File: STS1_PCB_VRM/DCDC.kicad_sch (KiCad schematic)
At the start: 25 parts, among them Q2 BSS123, U6 MP28167GQ

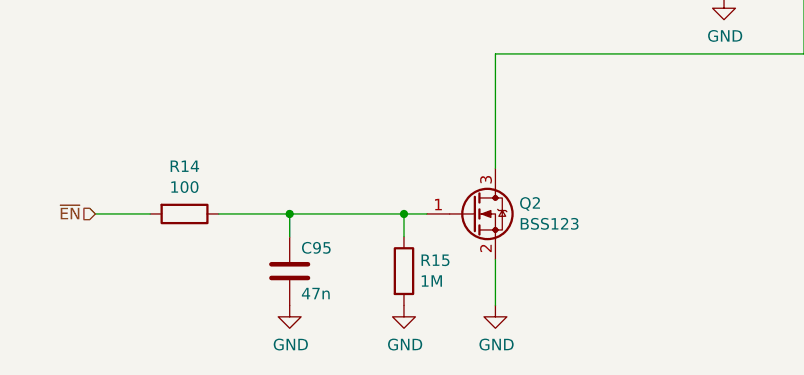
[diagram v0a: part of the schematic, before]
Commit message: Add a couple of Zener diodes to protect inputs of MOSFETs
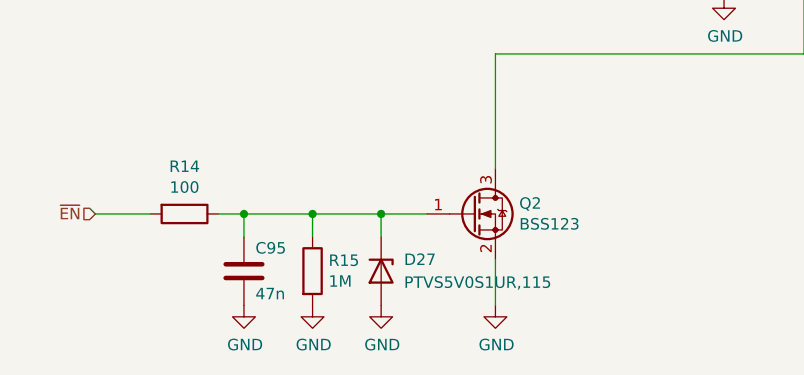
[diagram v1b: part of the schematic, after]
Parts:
- added D27: PTVS5V0S1UR,115, Diode_SMD:D_SOD-123, symbol Device:D_Zener
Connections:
- net GND: now also D27.2 (A)
- net at C95.1, Q2.1 (G), R14.1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: now also D27.1 (K)
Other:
- moved on the sheet: C95, R15
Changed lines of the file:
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@@
 (kicad_sch (version 20211123) (generator eeschema)
   (paper "A4")
-  (junction (at 57.15 102.87) (diameter 0) (color 0 0 0 0)
-  )
   (junction (at 125.73 96.52) (diameter 0) (color 0 0 0 0)
   )
@@
   (junction (at 105.41 73.66) (diameter 0) (color 0 0 0 0)
   )
+  (junction (at 54.61 102.87) (diameter 0) (color 0 0 0 0)
+  )
   (junction (at 105.41 60.96) (diameter 0) (color 0 0 0 0)
   )
+  (junction (at 46.99 102.87) (diameter 0) (color 0 0 0 0)
+  )
   (junction (at 238.76 82.55) (diameter 0) (color 0 0 0 0)
   )
+  (junction (at 39.37 102.87) (diameter 0) (color 0 0 0 0)
+  )
   (junction (at 114.3 73.66) (diameter 0) (color 0 0 0 0)
   )
   (junction (at 82.55 60.96) (diameter 0) (color 0 0 0 0)
   )
-  (junction (at 44.45 102.87) (diameter 0) (color 0 0 0 0)
-  )
   (junction (at 181.61 66.04) (diameter 0) (color 0 0 0 0)
   )
@@
   (junction (at 92.71 60.96) (diameter 0) (color 0 0 0 0)
   )
+  (wire (pts (xy 54.61 102.87) (xy 54.61 105.41))
+    (stroke (width 0) (type default) (color 0 0 0 0))
+  )
   (wire (pts (xy 179.07 77.47) (xy 194.31 77.47))
     (stroke (width 0) (type default) (color 0 0 0 0))
@@
     (stroke (width 0) (type default) (color 0 0 0 0))
   )
-  (wire (pts (xy 44.45 102.87) (xy 57.15 102.87))
-    (stroke (width 0) (type default) (color 0 0 0 0))
-  )
   (wire (pts (xy 191.77 82.55) (xy 203.2 82.55))
     (stroke (width 0) (type default) (color 0 0 0 0))
@@
     (stroke (width 0) (type default) (color 0 0 0 0))
   )
-  (wire (pts (xy 36.576 102.87) (xy 44.45 102.87))
+  (wire (pts (xy 46.99 102.87) (xy 54.61 102.87))
+    (stroke (width 0) (type default) (color 0 0 0 0))
+  )
+  (wire (pts (xy 36.576 102.87) (xy 39.37 102.87))
     (stroke (width 0) (type default) (color 0 0 0 0))
   )
@@
     (stroke (width 0) (type default) (color 0 0 0 0))
   )
+  (wire (pts (xy 54.61 102.87) (xy 59.69 102.87))
+    (stroke (width 0) (type default) (color 0 0 0 0))
+  )
   (wire (pts (xy 54.61 63.5) (xy 54.61 60.96))
     (stroke (width 0) (type default) (color 0 0 0 0))
@@
     (stroke (width 0) (type default) (color 0 0 0 0))
   )
+  (wire (pts (xy 39.37 102.87) (xy 46.99 102.87))
+    (stroke (width 0) (type default) (color 0 0 0 0))
+  )
   (wire (pts (xy 105.41 73.66) (xy 114.3 73.66))
     (stroke (width 0) (type default) (color 0 0 0 0))
@@
     (stroke (width 0) (type default) (color 0 0 0 0))
   )
-  (wire (pts (xy 44.45 102.87) (xy 44.45 105.41))
+  (wire (pts (xy 39.37 102.87) (xy 39.37 105.41))
     (stroke (width 0) (type default) (color 0 0 0 0))
   )
@@
     (stroke (width 0) (type default) (color 0 0 0 0))
   )
-  (wire (pts (xy 57.15 102.87) (xy 59.69 102.87))
-    (stroke (width 0) (type default) (color 0 0 0 0))
-  )
-  (wire (pts (xy 57.15 105.41) (xy 57.15 102.87))
+  (wire (pts (xy 46.99 105.41) (xy 46.99 102.87))
     (stroke (width 0) (type default) (color 0 0 0 0))
   )
@@
     (pin "2")
   )
-  (symbol (lib_id "Device:R") (at 57.15 109.22 0) (unit 1)
-    (in_bom yes) (on_board yes)
-    (property "Reference" "R15" (id 0) (at 58.928 108.0516 0)
-      (effects (font (size 1.27 1.27)) (justify left))
-    )
-    (property "Value" "1M" (id 1) (at 58.928 110.363 0)
-      (effects (font (size 1.27 1.27)) (justify left))
-    )
-    (property "Footprint" "Resistor_SMD:R_0603_1608Metric" (id 2) (at 55.372 109.22 90)
-      (effects (font (size 1.27 1.27)) hide)
-    )
-    (property "Datasheet" "~" (id 3) (at 57.15 109.22 0)
-      (effects (font (size 1.27 1.27)) hide)
-    )
-    (property "Manufacturer_Part_Number" "MR06X1004FTL " (id 4) (at 57.15 109.22 0)
+  (symbol (lib_id "Device:R") (at 46.99 109.22 0) (unit 1)
+    (in_bom yes) (on_board yes)
+    (property "Reference" "R15" (id 0) (at 48.768 108.0516 0)
+      (effects (font (size 1.27 1.27)) (justify left))
+    )
+    (property "Value" "1M" (id 1) (at 48.768 110.363 0)
+      (effects (font (size 1.27 1.27)) (justify left))
+    )
+    (property "Footprint" "Resistor_SMD:R_0603_1608Metric" (id 2) (at 45.212 109.22 90)
+      (effects (font (size 1.27 1.27)) hide)
+    )
+    (property "Datasheet" "~" (id 3) (at 46.99 109.22 0)
+      (effects (font (size 1.27 1.27)) hide)
+    )
+    (property "Manufacturer_Part_Number" "MR06X1004FTL " (id 4) (at 46.99 109.22 0)
       (effects (font (size 1.27 1.27)) hide)
     )
@@
     )
     (property "Manufacturer_Part_Number" "T491X107M025AT " (id 6) (at 226.06 88.9 0)
+      (effects (font (size 1.27 1.27)) hide)
+    )
+    (pin "1")
+    (pin "2")
+  )
+  (symbol (lib_id "Device:D_Zener") (at 54.61 109.22 270) (unit 1)
+    (in_bom yes) (on_board yes) (fields_autoplaced)
+    (property "Reference" "D27" (id 0) (at 57.15 107.9499 90)
+      (effects (font (size 1.27 1.27)) (justify left))
+    )
+    (property "Value" "PTVS5V0S1UR,115" (id 1) (at 57.15 110.4899 90)
+      (effects (font (size 0 0)) (justify left))
+    )
+    (property "Footprint" "Diode_SMD:D_SOD-123" (id 2) (at 54.61 109.22 0)
+      (effects (font (size 1.27 1.27)) hide)
+    )
+    (property "Datasheet" "~" (id 3) (at 54.61 109.22 0)
+      (effects (font (size 1.27 1.27)) hide)
+    )
+    (property "JLCPCB Part #" "C478011" (id 4) (at 54.61 109.22 0)
+      (effects (font (size 1.27 1.27)) hide)
+    )
+    (property "Manufacturer_Part_Number" "PTVS5V0S1UR,115 " (id 5) (at 54.61 109.22 0)
       (effects (font (size 1.27 1.27)) hide)
     )
@@
     (pin "1")
     (pin "2")
+  )
+  (symbol (lib_id "power:GND") (at 54.61 113.03 0) (unit 1)
+    (in_bom yes) (on_board yes)
+    (property "Reference" "#PWR077" (id 0) (at 54.61 119.38 0)
+      (effects (font (size 1.27 1.27)) hide)
+    )
+    (property "Value" "GND" (id 1) (at 54.737 117.4242 0))
+    (property "Footprint" "" (id 2) (at 54.61 113.03 0)
+      (effects (font (size 1.27 1.27)) hide)
+    )
+    (property "Datasheet" "" (id 3) (at 54.61 113.03 0)
+      (effects (font (size 1.27 1.27)) hide)
+    )
+    (pin "1")
   )
   (symbol (lib_id "power:GND") (at 121.92 83.82 0) (unit 1)
@@
     (pin "1")
   )
-  (symbol (lib_id "power:GND") (at 57.15 113.03 0) (unit 1)
-    (in_bom yes) (on_board yes)
-    (property "Reference" "#PWR04" (id 0) (at 57.15 119.38 0)
-      (effects (font (size 1.27 1.27)) hide)
-    )
-    (property "Value" "GND" (id 1) (at 57.277 117.4242 0))
-    (property "Footprint" "" (id 2) (at 57.15 113.03 0)
-      (effects (font (size 1.27 1.27)) hide)
-    )
-    (property "Datasheet" "" (id 3) (at 57.15 113.03 0)
-      (effects (font (size 1.27 1.27)) hide)
-    )
-    (pin "1")
-  )
-  (symbol (lib_id "Device:C") (at 44.45 109.22 0) (unit 1)
-    (in_bom yes) (on_board yes)
-    (property "Reference" "C95" (id 0) (at 45.72 106.68 0)
-      (effects (font (size 1.27 1.27)) (justify left))
-    )
-    (property "Value" "47n" (id 1) (at 45.72 111.76 0)
-      (effects (font (size 1.27 1.27)) (justify left))
-    )
-    (property "Footprint" "Capacitor_SMD:C_0603_1608Metric" (id 2) (at 45.4152 113.03 0)
-      (effects (font (size 1.27 1.27)) hide)
-    )
-    (property "Datasheet" "~" (id 3) (at 44.45 109.22 0)
-      (effects (font (size 1.27 1.27)) hide)
-    )
-    (property "Manufacturer_Part_Number" "CL10B473KB8VPJC " (id 4) (at 44.45 109.22 0)
+  (symbol (lib_id "power:GND") (at 46.99 113.03 0) (unit 1)
+    (in_bom yes) (on_board yes)
+    (property "Reference" "#PWR04" (id 0) (at 46.99 119.38 0)
+      (effects (font (size 1.27 1.27)) hide)
+    )
+    (property "Value" "GND" (id 1) (at 47.117 117.4242 0))
+    (property "Footprint" "" (id 2) (at 46.99 113.03 0)
+      (effects (font (size 1.27 1.27)) hide)
+    )
+    (property "Datasheet" "" (id 3) (at 46.99 113.03 0)
+      (effects (font (size 1.27 1.27)) hide)
+    )
+    (pin "1")
+  )
+  (symbol (lib_id "Device:C") (at 39.37 109.22 0) (unit 1)
+    (in_bom yes) (on_board yes)
+    (property "Reference" "C95" (id 0) (at 40.64 106.68 0)
+      (effects (font (size 1.27 1.27)) (justify left))
+    )
+    (property "Value" "47n" (id 1) (at 40.64 111.76 0)
+      (effects (font (size 1.27 1.27)) (justify left))
+    )
+    (property "Footprint" "Capacitor_SMD:C_0603_1608Metric" (id 2) (at 40.3352 113.03 0)
+      (effects (font (size 1.27 1.27)) hide)
+    )
+    (property "Datasheet" "~" (id 3) (at 39.37 109.22 0)
+      (effects (font (size 1.27 1.27)) hide)
+    )
+    (property "Manufacturer_Part_Number" "CL10B473KB8VPJC " (id 4) (at 39.37 109.22 0)
       (effects (font (size 1.27 1.27)) hide)
     )
@@
     (pin "2")
   )
-  (symbol (lib_id "power:GND") (at 44.45 113.03 0) (unit 1)
-    (in_bom yes) (on_board yes)
-    (property "Reference" "#PWR063" (id 0) (at 44.45 119.38 0)
-      (effects (font (size 1.27 1.27)) hide)
-    )
-    (property "Value" "GND" (id 1) (at 44.577 117.4242 0))
-    (property "Footprint" "" (id 2) (at 44.45 113.03 0)
-      (effects (font (size 1.27 1.27)) hide)
-    )
-    (property "Datasheet" "" (id 3) (at 44.45 113.03 0)
-      (effects (font (size 1.27 1.27)) hide)
-    )
+  (symbol (lib_id "power:GND") (at 39.37 113.03 0) (unit 1)
+    (in_bom yes) (on_board yes)
+    (property "Reference" "#PWR063" (id 0) (at 39.37 119.38 0)
+      (effects (font (size 1.27 1.27)) hide)
+    )
+    (property "Value" "GND" (id 1) (at 39.497 117.4242 0))
+    (property "Footprint" "" (id 2) (at 39.37 113.03 0)
+      (effects (font (size 1.27 1.27)) hide)
+    )
+    (property "Datasheet" "" (id 3) (at 39.37 113.03 0)
+      (effects (font (size 1.27 1.27)) hide)
+    )

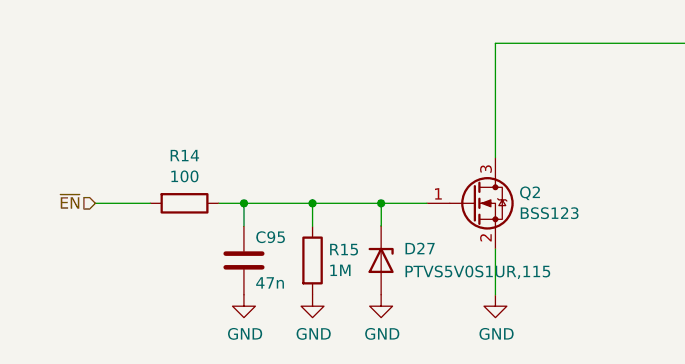
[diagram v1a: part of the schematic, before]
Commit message: Increase delay before RTD toggles the DC-DC converter on and off: C95 47 nF -> 4.7 uF
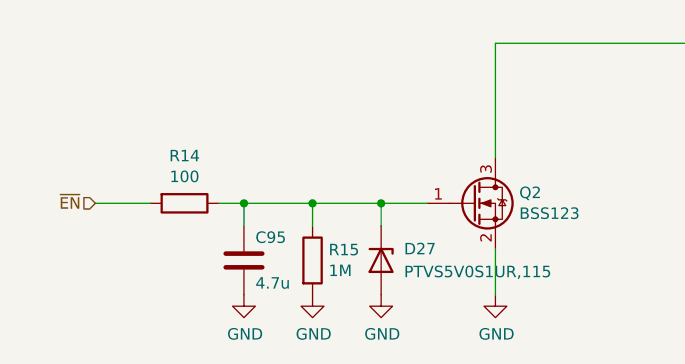
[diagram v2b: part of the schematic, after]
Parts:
- C95: value 47n -> 4.7u; JLCPCB Part # (none) -> C5969198; Manufacturer_Part_Number CL10B473KB8VPJC -> CL10A475KP8NNWC
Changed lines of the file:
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@@
       (effects (font (size 1.27 1.27)) (justify left))
     )
-    (property "Value" "47n" (id 1) (at 40.64 111.76 0)
+    (property "Value" "4.7u" (id 1) (at 40.64 111.76 0)
       (effects (font (size 1.27 1.27)) (justify left))
     )
@@
       (effects (font (size 1.27 1.27)) hide)
     )
-    (property "Manufacturer_Part_Number" "CL10B473KB8VPJC " (id 4) (at 39.37 109.22 0)
+    (property "Manufacturer_Part_Number" "CL10A475KP8NNWC " (id 4) (at 39.37 109.22 0)
       (effects (font (size 1.27 1.27)) hide)
     )
+    (property "JLCPCB Part #" "C5969198" (id 5) (at 39.37 109.22 0)
+      (effects (font (size 1.27 1.27)) hide)
+    )

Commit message: Update the manufacturer part number for some of components to be compatible with avaiable parts in the JLC parts database
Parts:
- C37: JLCPCB Part # C2980159 -> C2762594; Manufacturer_Part_Number CL10A226MP8NRNC -> CL10A226MO7JZNC
- C38, C42, C43, C44: JLCPCB Part # C1591 -> C129621; Manufacturer_Part_Number CL10B104KB8NNNC -> C0603C104K5RACAUTO
- C39, C40, C79: JLCPCB Part # C307479 -> C342956; Manufacturer_Part_Number CL10B105KA8NFNC -> CGA3E1X7R1V105KT000N
- C41: JLCPCB Part # C307486 -> C561824; Manufacturer_Part_Number CL10B223KB8NFNC -> C0603C223K5RACAUTO
- C45, C46: JLCPCB Part # (none) -> C2959727; Manufacturer_Part_Number CL10A106KP8NQSC -> GRM188Z71A106KA73D
- C95: JLCPCB Part # C5969198 -> C338087; Manufacturer_Part_Number CL10A475KP8NNWC -> CGA3E1X5R0J475KT0Y0E
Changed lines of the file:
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@@
       (effects (font (size 1.27 1.27)) (justify left))
     )
-    (property "Manufacturer_Part_Number" "CL10A106KP8NQSC " (id 5) (at 214.63 88.9 0)
+    (property "Manufacturer_Part_Number" "GRM188Z71A106KA73D" (id 5) (at 214.63 88.9 0)
+      (effects (font (size 1.27 1.27)) hide)
+    )
+    (property "JLCPCB Part #" "C2959727" (id 6) (at 214.63 88.9 0)
       (effects (font (size 1.27 1.27)) hide)
     )
@@
       (effects (font (size 1.27 1.27)) hide)
     )
-    (property "JLCPCB Part #" "C307479" (id 4) (at 114.3 80.01 0)
-      (effects (font (size 1.27 1.27)) hide)
-    )
-    (property "Manufacturer_Part_Number" "CL10B105KA8NFNC " (id 5) (at 114.3 80.01 0)
+    (property "JLCPCB Part #" "C342956" (id 4) (at 114.3 80.01 0)
+      (effects (font (size 1.27 1.27)) hide)
+    )
+    (property "Manufacturer_Part_Number" "CGA3E1X7R1V105KT000N" (id 5) (at 114.3 80.01 0)
       (effects (font (size 1.27 1.27)) hide)
     )
@@
       (effects (font (size 1.27 1.27)) (justify left))
     )
-    (property "Manufacturer_Part_Number" "CL10A106KP8NQSC " (id 5) (at 203.2 88.9 0)
+    (property "Manufacturer_Part_Number" "GRM188Z71A106KA73D" (id 5) (at 203.2 88.9 0)
+      (effects (font (size 1.27 1.27)) hide)
+    )
+    (property "JLCPCB Part #" "C2959727" (id 6) (at 203.2 88.9 0)
       (effects (font (size 1.27 1.27)) hide)
     )
@@
       (effects (font (size 1.27 1.27)) hide)
     )
-    (property "JLCPCB Part #" "C1591" (id 4) (at 191.77 88.9 0)
-      (effects (font (size 1.27 1.27)) hide)
-    )
-    (property "Manufacturer_Part_Number" "CL10B104KB8NNNC " (id 5) (at 191.77 88.9 0)
+    (property "JLCPCB Part #" "C129621" (id 4) (at 191.77 88.9 0)
+      (effects (font (size 1.27 1.27)) hide)
+    )
+    (property "Manufacturer_Part_Number" "C0603C104K5RACAUTO" (id 5) (at 191.77 88.9 0)
       (effects (font (size 1.27 1.27)) hide)
     )
@@
       (effects (font (size 1.27 1.27)) hide)
     )
-    (property "JLCPCB Part #" "C1591" (id 4) (at 175.26 60.96 0)
-      (effects (font (size 1.27 1.27)) hide)
-    )
-    (property "Manufacturer_Part_Number" "CL10B104KB8NNNC " (id 5) (at 175.26 60.96 0)
+    (property "JLCPCB Part #" "C129621" (id 4) (at 175.26 60.96 0)
+      (effects (font (size 1.27 1.27)) hide)
+    )
+    (property "Manufacturer_Part_Number" "C0603C104K5RACAUTO" (id 5) (at 175.26 60.96 0)
       (effects (font (size 1.27 1.27)) hide)
     )
@@
       (effects (font (size 1.27 1.27)) hide)
     )
-    (property "JLCPCB Part #" "C307479" (id 6) (at 92.71 74.93 0)
-      (effects (font (size 1.27 1.27)) hide)
-    )
-    (property "Manufacturer_Part_Number" "CL10B105KA8NFNC " (id 7) (at 92.71 74.93 0)
+    (property "JLCPCB Part #" "C342956" (id 6) (at 92.71 74.93 0)
+      (effects (font (size 1.27 1.27)) hide)
+    )
+    (property "Manufacturer_Part_Number" "CGA3E1X7R1V105KT000N" (id 7) (at 92.71 74.93 0)
       (effects (font (size 1.27 1.27)) hide)
     )
@@
       (effects (font (size 1.27 1.27)) (justify left))
     )
-    (property "JLCPCB Part #" "C2980159" (id 5) (at 68.58 67.31 0)
-      (effects (font (size 1.27 1.27)) hide)
-    )
-    (property "Manufacturer_Part_Number" "CL10A226MP8NRNC " (id 6) (at 68.58 67.31 0)
+    (property "JLCPCB Part #" "C2762594" (id 5) (at 68.58 67.31 0)
+      (effects (font (size 1.27 1.27)) hide)
+    )
+    (property "Manufacturer_Part_Number" "CL10A226MO7JZNC" (id 6) (at 68.58 67.31 0)
       (effects (font (size 1.27 1.27)) hide)
     )
@@
       (effects (font (size 1.27 1.27)) hide)
     )
-    (property "JLCPCB Part #" "C307486" (id 4) (at 125.73 102.87 0)
-      (effects (font (size 1.27 1.27)) hide)
-    )
-    (property "Manufacturer_Part_Number" "CL10B223KB8NFNC " (id 5) (at 125.73 102.87 0)
+    (property "JLCPCB Part #" "C561824" (id 4) (at 125.73 102.87 0)
+      (effects (font (size 1.27 1.27)) hide)
+    )
+    (property "Manufacturer_Part_Number" "C0603C223K5RACAUTO" (id 5) (at 125.73 102.87 0)
       (effects (font (size 1.27 1.27)) hide)
     )
@@
       (effects (font (size 1.27 1.27)) (justify left))
     )
-    (property "JLCPCB Part #" "C307479" (id 5) (at 121.92 80.01 0)
-      (effects (font (size 1.27 1.27)) hide)
-    )
-    (property "Manufacturer_Part_Number" "CL10B105KA8NFNC " (id 6) (at 121.92 80.01 0)
+    (property "JLCPCB Part #" "C342956" (id 5) (at 121.92 80.01 0)
+      (effects (font (size 1.27 1.27)) hide)
+    )
+    (property "Manufacturer_Part_Number" "CGA3E1X7R1V105KT000N" (id 6) (at 121.92 80.01 0)
       (effects (font (size 1.27 1.27)) hide)
     )
@@
       (effects (font (size 1.27 1.27)) hide)
     )
-    (property "JLCPCB Part #" "C1591" (id 4) (at 175.26 77.47 0)
-      (effects (font (size 1.27 1.27)) hide)
-    )
-    (property "Manufacturer_Part_Number" "CL10B104KB8NNNC " (id 5) (at 175.26 77.47 0)
+    (property "JLCPCB Part #" "C129621" (id 4) (at 175.26 77.47 0)
+      (effects (font (size 1.27 1.27)) hide)
+    )
+    (property "Manufacturer_Part_Number" "C0603C104K5RACAUTO" (id 5) (at 175.26 77.47 0)
       (effects (font (size 1.27 1.27)) hide)
     )
@@
       (effects (font (size 1.27 1.27)) hide)
     )
-    (property "JLCPCB Part #" "C1591" (id 4) (at 82.55 67.31 0)
-      (effects (font (size 1.27 1.27)) hide)
-    )
-    (property "Manufacturer_Part_Number" "CL10B104KB8NNNC " (id 5) (at 82.55 67.31 0)
+    (property "JLCPCB Part #" "C129621" (id 4) (at 82.55 67.31 0)
+      (effects (font (size 1.27 1.27)) hide)
+    )
+    (property "Manufacturer_Part_Number" "C0603C104K5RACAUTO" (id 5) (at 82.55 67.31 0)
       (effects (font (size 1.27 1.27)) hide)
     )
@@
       (effects (font (size 1.27 1.27)) hide)
     )
-    (property "Manufacturer_Part_Number" "CL10A475KP8NNWC " (id 4) (at 39.37 109.22 0)
-      (effects (font (size 1.27 1.27)) hide)
-    )
-    (property "JLCPCB Part #" "C5969198" (id 5) (at 39.37 109.22 0)
-      (effects (font (size 1.27 1.27)) hide)
-    )
+    (property "Manufacturer_Part_Number" "CGA3E1X5R0J475KT0Y0E" (id 4) (at 39.37 109.22 0)
+      (effects (font (size 1.27 1.27)) hide)
+    )
+    (property "JLCPCB Part #" "C338087" (id 5) (at 39.37 109.22 0)
+      (effects (font (size 1.27 1.27)) hide)
+    )
